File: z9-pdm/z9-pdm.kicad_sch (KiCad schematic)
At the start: 8 parts

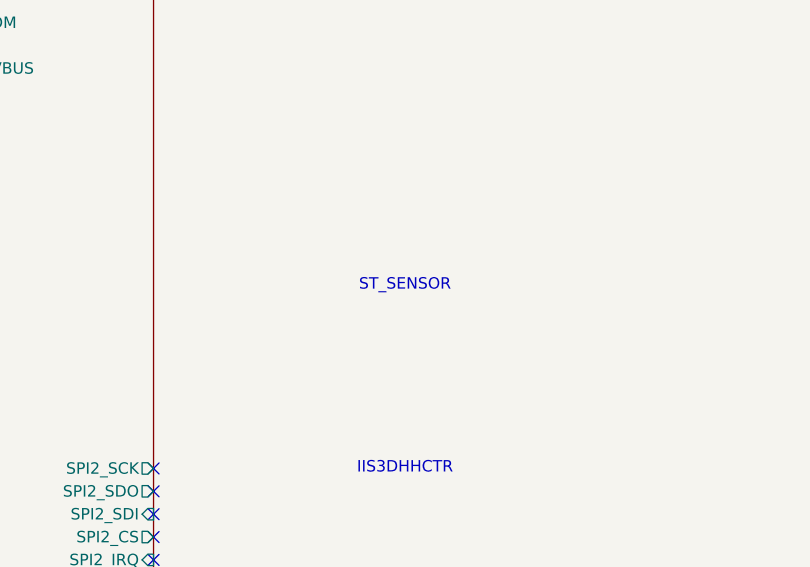
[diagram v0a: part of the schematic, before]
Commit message: Remove unused ST_SENSOR text from schematic
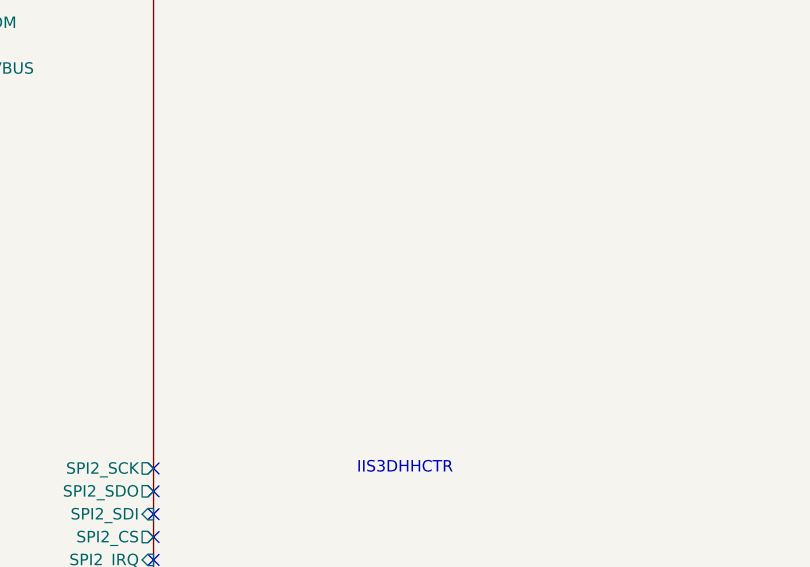
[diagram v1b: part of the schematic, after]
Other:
- note removed: "ST_SENSOR"
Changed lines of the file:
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@@
 		(company "DNT")
-	)
-	(text "ST_SENSOR"
-		(exclude_from_sim no)
-		(at 219.71 68.58 0)
-		(effects
-			(font
-				(size 1.27 1.27)
-			)
-		)
 	)
 	(text "IIS3DHHCTR"

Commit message: mainly route vip
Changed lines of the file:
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@@
 		)
 	)
-	(label "HC_5"
+	(label "HC_2"
 		(at 304.8 50.8 180)
 		(effects
@@
 		)
 	)
-	(label "HC_4"
+	(label "HC_3"
 		(at 304.8 46.99 180)
 		(effects
@@
 		)
 	)
-	(label "HC_3"
+	(label "HC_4"
 		(at 304.8 43.18 180)
 		(effects
@@
 		)
 	)
-	(label "HC_1"
+	(label "HC_6"
 		(at 304.8 35.56 180)
 		(effects
@@
 		)
 	)
-	(label "HC_2"
+	(label "HC_5"
 		(at 304.8 39.37 180)
 		(effects
@@
 		)
 	)
-	(label "HC_6"
+	(label "HC_1"
 		(at 304.8 54.61 180)
 		(effects
